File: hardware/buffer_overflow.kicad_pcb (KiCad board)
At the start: 2 copper layers, 37.5 x 49.2 mm, 30 parts, among them U1 LM741

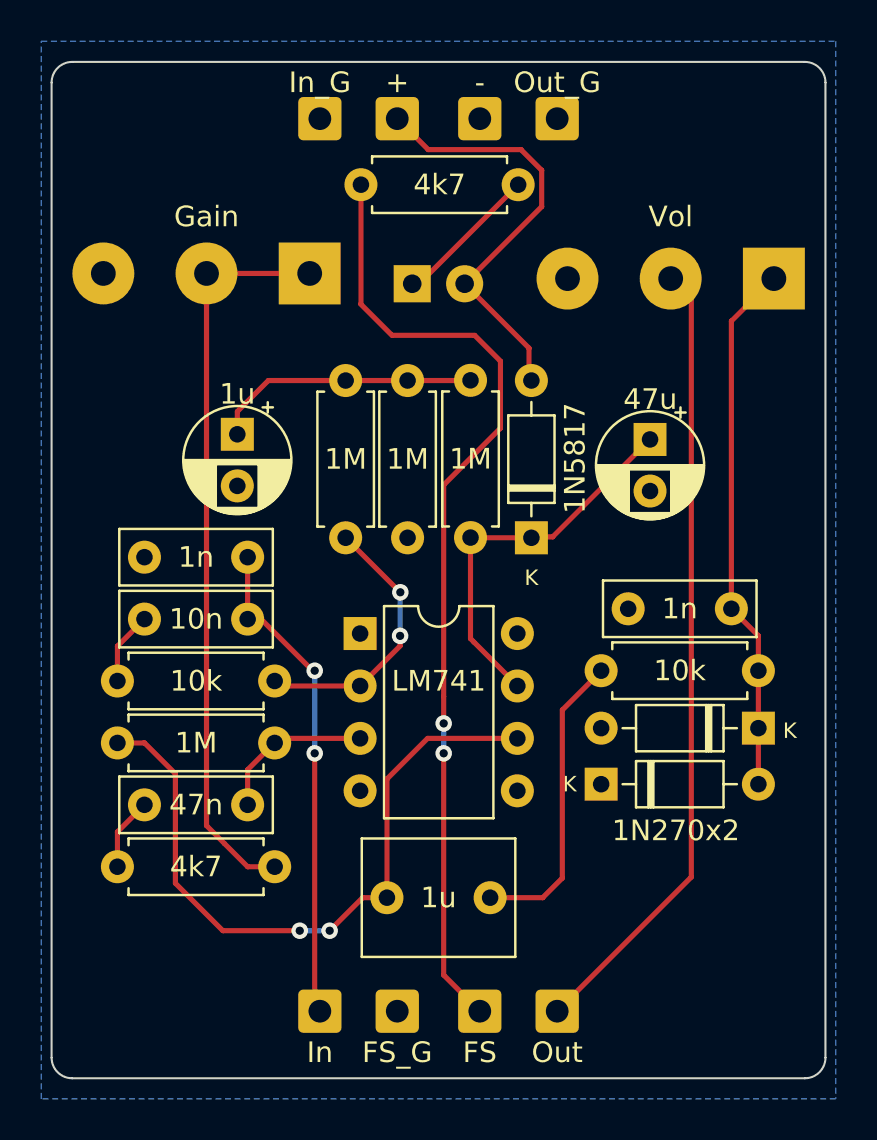
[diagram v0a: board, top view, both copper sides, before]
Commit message: Fix issues identified in v0.01
Bugfixes:
 - Reverse swapped opamp inputs
 - Reverse backwards Volume potentiometer

Enhancements:
 - Cosmetic and functional updates to silkscreen
 - Include revision and github reference
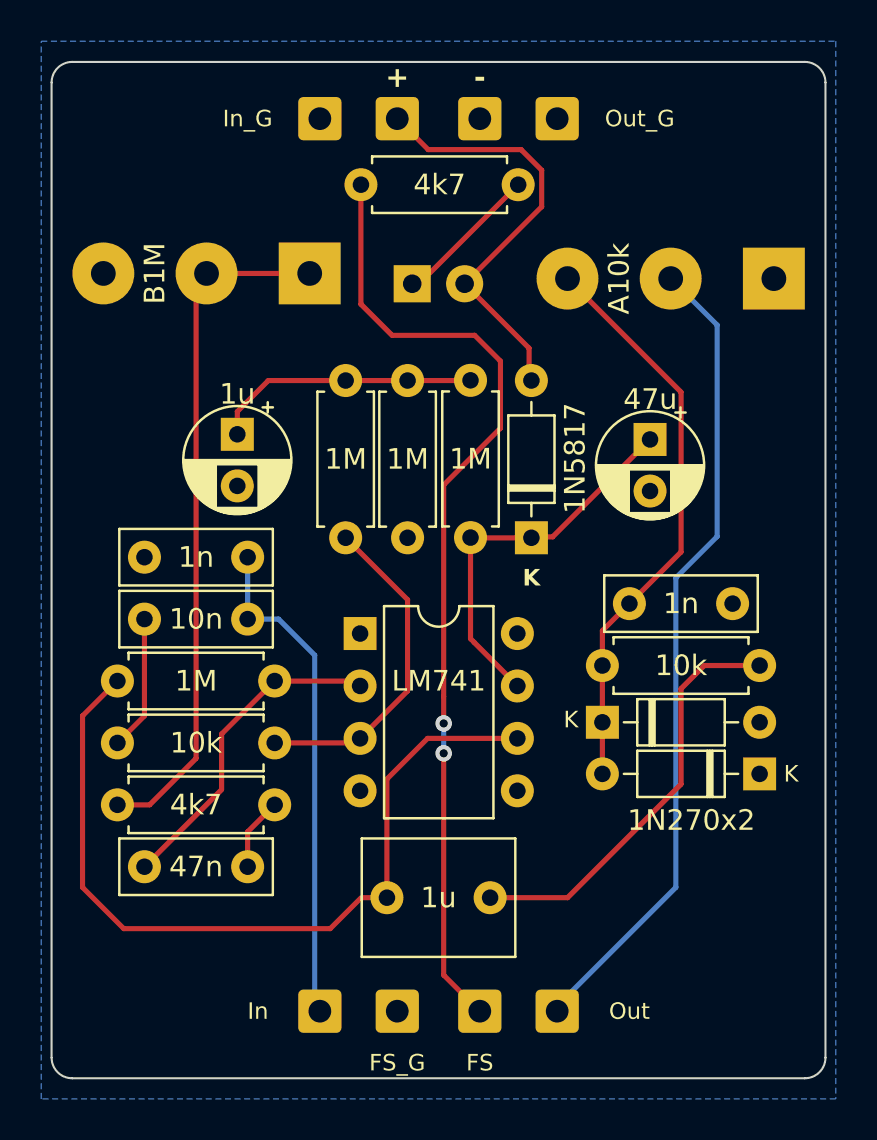
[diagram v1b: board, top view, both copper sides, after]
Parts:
- D4: value 270 -> 1N270
- moved D3 7.70 mm to (76.8, 58.0), turned to 180 degrees
- moved D4 7.57 mm to (69.2, 55.5), turned to 0 degrees
- moved R8 7.56 mm to (69.2, 52.8), turned to 0 degrees
- moved C7 5.07 mm to (75.5, 49.8), turned to 180 degrees
- moved C4 3.00 mm to (52.0, 62.5)
- moved R2 3.00 mm to (45.7, 56.5)
- moved R6 3.00 mm to (53.3, 59.5)
- moved R7 3.00 mm to (45.7, 53.5)
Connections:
- C4 pad 1: /741_NonInv -> Net-(C4-Pad1)
- C4 pad 2: Net-(C4-Pad2) -> /741_Inv
- R2 pad 2: /741_Inv -> /741_NonInv
- R3 pad 1: /741_Inv -> /741_NonInv
- R6 pad 1: /GAIN_CTL -> Net-(C4-Pad1)
- R6 pad 2: Net-(C4-Pad2) -> /GAIN_CTL
- R7 pad 2: /741_NonInv -> /741_Inv
- Vol pad 1: /PRE_VOLUME -> GND
- Vol pad 3: GND -> /PRE_VOLUME
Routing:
- net /741_NonInv: track 7.78 -> 16.1 mm
- net /741_OUT: track 33.5 -> 39.7 mm, vias 2 -> 0
- net Net-(C6-Pad2): track 14.7 -> 20.4 mm
- net Net-(C4-Pad2): track 3.54 -> 0.00 mm
- net Net-(C4-Pad1): track 0.00 -> 3.54 mm
- net Net-(C3-Pad2): track 3.54 -> 6.54 mm
- net /741_Inv: track 13.3 -> 15.9 mm, vias 2 -> 0
- net /GAIN_CTL: track 35.9 -> 33.5 mm
- net /PRE_VOLUME: track 25.9 -> 27.9 mm
- net /OUTPUT_TIP: track 38.6 -> 39.6 mm
- net /INPUT_TIP: track 23.9 -> 24.3 mm, vias 2 -> 0
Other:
- board text added: "github.com/whbeers/buffer_overflow"
- board text added: "v0.1"

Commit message: fix alignment of potentiometers
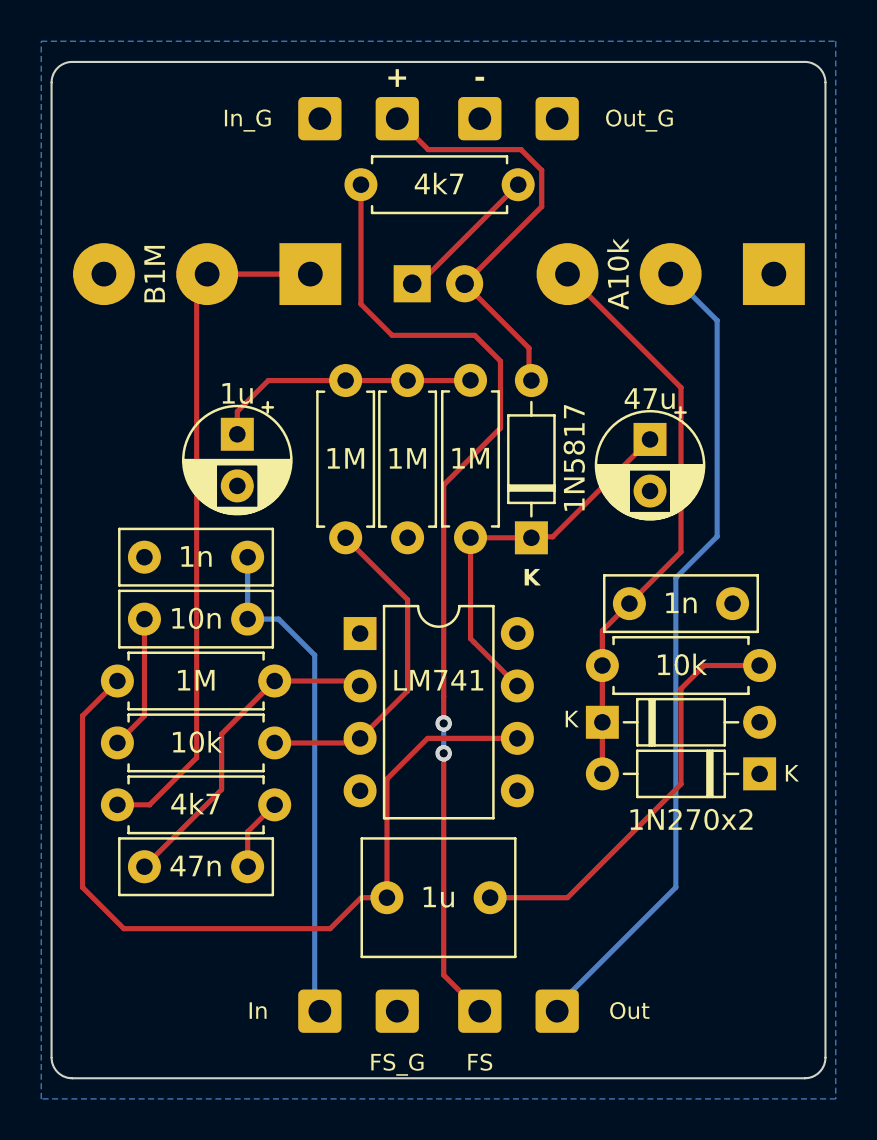
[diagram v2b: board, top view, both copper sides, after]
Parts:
- moved Vol 0.22 mm to (72.5, 30.0)
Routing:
- net /GAIN_CTL: track 33.5 -> 34.2 mm
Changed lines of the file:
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@@
   )
   (footprint "buffer_overflow:Potentiometer_Single_3_Horizontal" (layer "B.Cu")
-    (at 72.4925 30.19 180)
+    (at 72.4925 29.972 180)
     (property "Sheetfile" "buffer_overflow.kicad_sch")
     (property "Sheetname" "")
@@
   )
   (footprint "buffer_overflow:Potentiometer_Single_3_Horizontal" (layer "B.Cu")
-    (at 50 29.94 180)
+    (at 50.0305 29.972 180)
     (property "Sheetfile" "buffer_overflow.kicad_sch")
     (property "Sheetname" "")
@@
   (segment (start 57.5745 64) (end 58.75 64) (width 0.25) (layer "F.Cu") (net 8))
   (segment (start 69.19 58) (end 69.19 51.06) (width 0.25) (layer "F.Cu") (net 9))
-  (segment (start 73 47.25) (end 73 39.5) (width 0.25) (layer "F.Cu") (net 9))
   (segment (start 69.19 51.06) (end 70.5 49.75) (width 0.25) (layer "F.Cu") (net 9))
-  (segment (start 73 39.5) (end 67.5 34) (width 0.25) (layer "F.Cu") (net 9))
-  (segment (start 70.5 49.75) (end 73 47.25) (width 0.25) (layer "F.Cu") (net 9))
-  (segment (start 55.0075 33.75) (end 50.0075 33.75) (width 0.25) (layer "F.Cu") (net 10))
-  (segment (start 45.69 59.5) (end 47.25 59.5) (width 0.25) (layer "F.Cu") (net 10))
-  (segment (start 47.25 59.5) (end 49.5 57.25) (width 0.25) (layer "F.Cu") (net 10))
-  (segment (start 49.5 57.25) (end 49.5 34.2575) (width 0.25) (layer "F.Cu") (net 10))
+  (segment (start 67.5 33.782) (end 73 39.282) (width 0.25) (layer "F.Cu") (net 9))
+  (segment (start 73 39.282) (end 73 47.25) (width 0.25) (layer "F.Cu") (net 9))
+  (segment (start 73 47.25) (end 70.5 49.75) (width 0.25) (layer "F.Cu") (net 9))
+  (segment (start 49.53 57.22) (end 47.25 59.5) (width 0.25) (layer "F.Cu") (net 10))
+  (segment (start 50.038 33.782) (end 49.53 34.29) (width 0.25) (layer "F.Cu") (net 10))
+  (segment (start 47.25 59.5) (end 45.69 59.5) (width 0.25) (layer "F.Cu") (net 10))
+  (segment (start 49.53 34.29) (end 49.53 57.22) (width 0.25) (layer "F.Cu") (net 10))
   (segment (start 49.5 34.2575) (end 50.0075 33.75) (width 0.25) (layer "F.Cu") (net 10))
+  (segment (start 50.038 33.782) (end 55.038 33.782) (width 0.25) (layer "F.Cu") (net 10))
   (segment (start 50.737299 58.762701) (end 47 62.5) (width 0.25) (layer "F.Cu") (net 11))
   (segment (start 57.21 53.5) (end 57.45 53.74) (width 0.25) (layer "F.Cu") (net 11))
@@
   (segment (start 60.75 27.75) (end 59.25 26.25) (width 0.25) (layer "F.Cu") (net 14))
   (segment (start 66.25 30.515) (end 66.25 28.75) (width 0.25) (layer "F.Cu") (net 14))
-  (segment (start 74.75 46.5) (end 74.75 36.25) (width 0.25) (layer "B.Cu") (net 15))
-  (segment (start 74.75 36.25) (end 72.5 34) (width 0.25) (layer "B.Cu") (net 15))
+  (segment (start 67 69.25) (end 72.75 63.5) (width 0.25) (layer "B.Cu") (net 15))
   (segment (start 72.75 63.5) (end 72.75 48.5) (width 0.25) (layer "B.Cu") (net 15))
+  (segment (start 74.75 46.5) (end 74.75 36.032) (width 0.25) (layer "B.Cu") (net 15))
   (segment (start 72.75 48.5) (end 74.75 46.5) (width 0.25) (layer "B.Cu") (net 15))
   (segment (start 67 69.5) (end 67 69.25) (width 0.25) (layer "B.Cu") (net 15))
-  (segment (start 67 69.25) (end 72.75 63.5) (width 0.25) (layer "B.Cu") (net 15))
+  (segment (start 74.75 36.032) (end 72.5 33.782) (width 0.25) (layer "B.Cu") (net 15))
   (segment (start 61.5 67.75) (end 63.25 69.5) (width 0.25) (layer "F.Cu") (net 16))
   (segment (start 64.25 38) (end 64.25 41.25) (width 0.25) (layer "F.Cu") (net 16))

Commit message: Mostly cosmetic updates
 - replace LED footprint with 3mm non-flat
 - shift text around
 - fix grid alignment for edge cuts
 - misc text updates
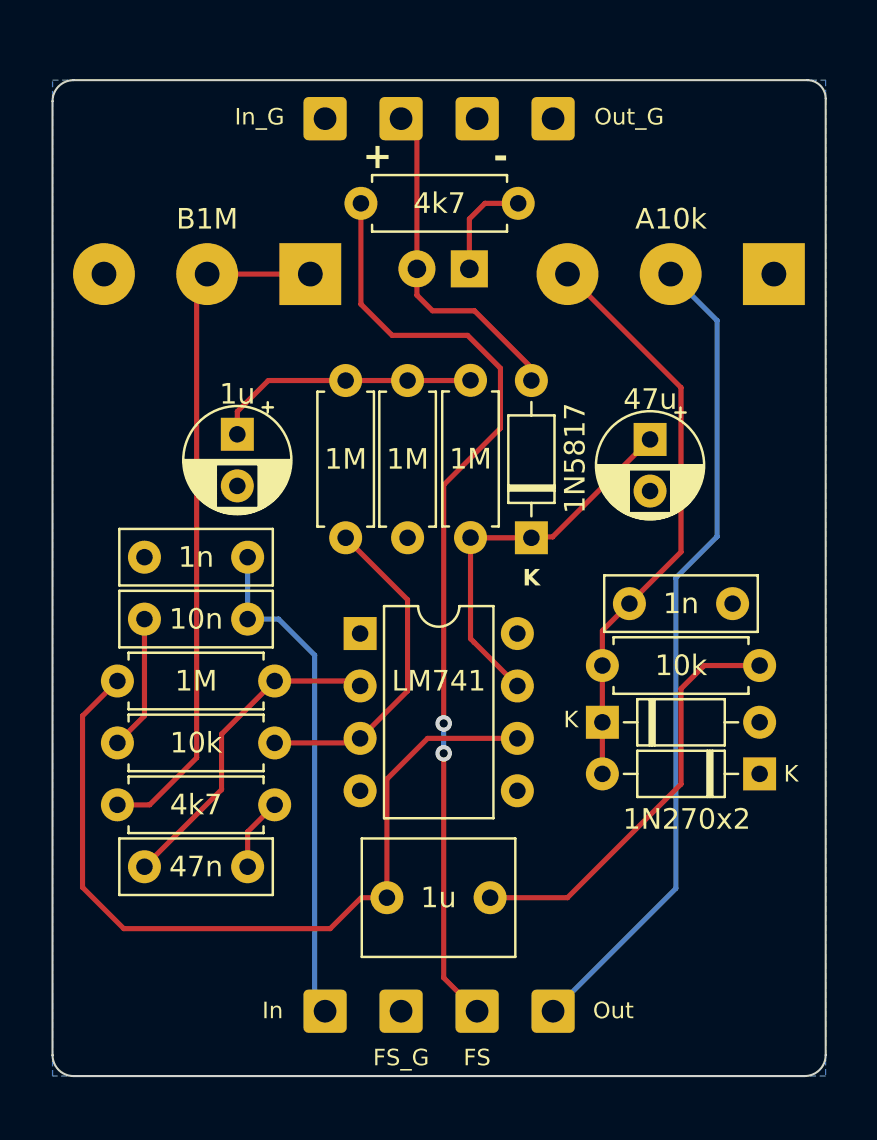
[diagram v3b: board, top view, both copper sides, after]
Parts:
- D2: footprint LED_THT:LED_D5.0mm_FlatTop -> LED_THT:LED_D3.0mm
- D3: value 1N270x2 -> 1N270
- moved D2 2.86 mm to (62.7, 33.5), turned to 180 degrees
- moved R1 0.90 mm to (65.1, 30.4)
- moved J1 0.25 mm to (55.8, 69.5)
- moved J5 0.25 mm to (55.8, 26.2)
- moved J2 0.20 mm to (66.8, 69.5)
- moved J6 0.20 mm to (66.8, 26.2)
- moved J3 0.19 mm to (59.4, 26.2)
- moved J8 0.19 mm to (59.4, 69.5)
- moved J4 0.13 mm to (63.1, 69.5)
- moved J7 0.13 mm to (63.1, 26.2)
- renumbered In to J1, Out to J2, + to J3, FS to J4, In_G to J5, Out_G to J6, - to J7, FS_G to J8, Vol to POT1, Gain to POT2
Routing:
- net /DC_SHIELD: track 21.1 -> 17.8 mm
- net Net-(D2-K): track 6.79 -> 5.10 mm
- net /Footswitch: track 47.1 -> 45.9 mm
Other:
- board size 37.5 x 49.2 mm -> 37.5 x 48.3 mm
- board text added: "${COMMENT1}"
- board text added: "${REVISION}"
- board text removed: "github.com/whbeers/buffer_overflow"
- board text removed: "v0.1"
